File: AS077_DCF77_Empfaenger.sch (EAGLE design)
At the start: 82 parts, among them IC1 CA3130E, IC2 4093N, IC3 4538N, IC4 4093N, J1 Rückkopplung, J2 JUMPER_J5MM, J3 JUMPER_J5MM, Q1 34MM_PIEZO, T1 BC549C, T2 BF244A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

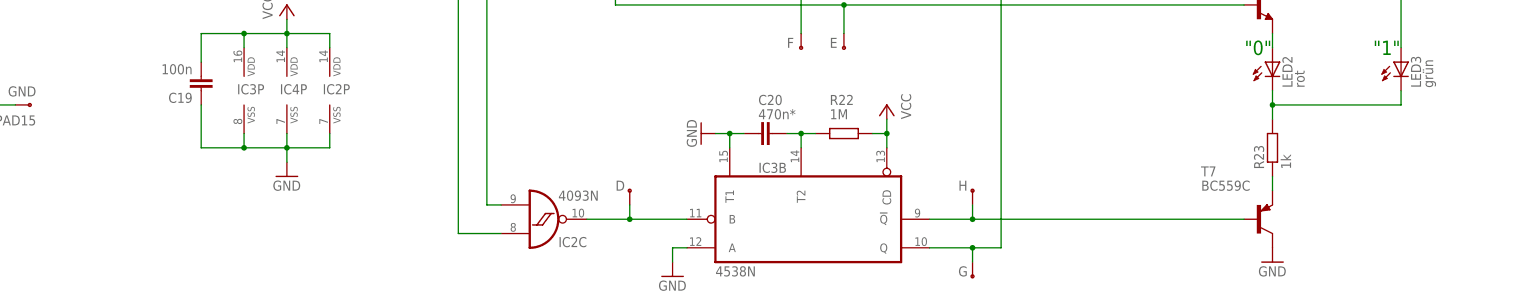
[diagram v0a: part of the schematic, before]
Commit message: * Renamed included library * Changed all references to new lib name
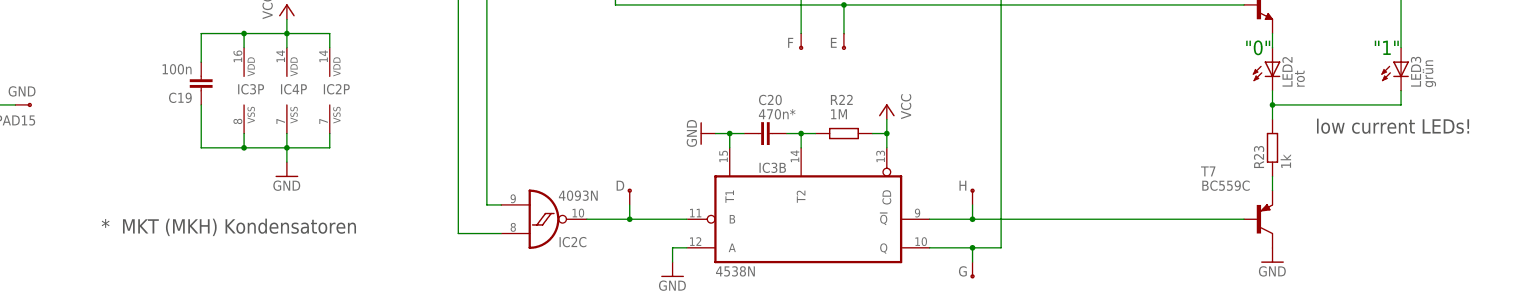
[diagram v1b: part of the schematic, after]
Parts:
- C1, C10, C16, C17, C19, C2, C4, C5, C6, C9: device 0027 DCF77-Empfänger:RCL_C-EU050-024X044 -> AS077_DCF77_Empfaenger:RCL_C-EU050-024X044
- C11, C13, C14, C15, C20, C7: device 0027 DCF77-Empfänger:RCL_C-EU075-032X103 -> AS077_DCF77_Empfaenger:RCL_C-EU075-032X103
- C12: device 0027 DCF77-Empfänger:RCL_CPOL-EUE5-6 -> AS077_DCF77_Empfaenger:RCL_CPOL-EUE5-6
- C18, C3: device 0027 DCF77-Empfänger:RCL_CPOL-EUE5-10.5 -> AS077_DCF77_Empfaenger:RCL_CPOL-EUE5-10.5
- C8: device 0027 DCF77-Empfänger:RCL_C-TRIMM808-7.5 -> AS077_DCF77_Empfaenger:RCL_C-TRIMM808-7.5
- D1, D2: device 0027 DCF77-Empfänger:DIODE_AA112 -> AS077_DCF77_Empfaenger:DIODE_AA112
- IC1: device 0027 DCF77-Empfänger:CA3130N -> AS077_DCF77_Empfaenger:CA3130N
- IC2, IC4: device 0027 DCF77-Empfänger:40XX_4093N -> AS077_DCF77_Empfaenger:40XX_4093N
- IC3: device 0027 DCF77-Empfänger:45XX_4538N -> AS077_DCF77_Empfaenger:45XX_4538N
- J1, J2, J3: device 0027 DCF77-Empfänger:JUMPER_J5MM -> AS077_DCF77_Empfaenger:JUMPER_J5MM
- LED1, LED2, LED3: device 0027 DCF77-Empfänger:LED_LED5MM -> AS077_DCF77_Empfaenger:LED_LED5MM
- PAD1, PAD10, PAD11, PAD12, PAD13, PAD14, PAD15, PAD16, PAD17, PAD18, PAD2, PAD3, PAD4, PAD5, PAD6, PAD7, PAD8, PAD9: device 0027 DCF77-Empfänger:WIREPAD_2.2/1.3 -> AS077_DCF77_Empfaenger:WIREPAD_2.2/1.3
- Q1: device 0027 DCF77-Empfänger:34MM_PIEZO -> AS077_DCF77_Empfaenger:34MM_PIEZO
- R1, R10, R11, R12, R13, R14, R15, R16, R19, R2, R20, R21, R4, R5, R6, R7, R8, R9: device 0027 DCF77-Empfänger:RCL_R-EU_0207/5V -> AS077_DCF77_Empfaenger:RCL_R-EU_0207/5V
- R17, R18, R22, R3: device 0027 DCF77-Empfänger:RCL_R-EU_0207/15 -> AS077_DCF77_Empfaenger:RCL_R-EU_0207/15
- R23: device 0027 DCF77-Empfänger:RCL_R-EU_0207/10 -> AS077_DCF77_Empfaenger:RCL_R-EU_0207/10
- T1, T3, T4: device 0027 DCF77-Empfänger:BC549C5.08 -> AS077_DCF77_Empfaenger:BC549C5.08
- T2: device 0027 DCF77-Empfänger:BF244A5.08 -> AS077_DCF77_Empfaenger:BF244A5.08
- T5, T6: device 0027 DCF77-Empfänger:BC549C2.54 -> AS077_DCF77_Empfaenger:BC549C2.54
- T7: device 0027 DCF77-Empfänger:BC559C5.08 -> AS077_DCF77_Empfaenger:BC559C5.08
- U$1: device 0027 DCF77-Empfänger:9V_SILKSCREEN -> AS077_DCF77_Empfaenger:9V_SILKSCREEN
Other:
- note added: "* MKT (MKH) Kondensatoren"
- note added: "low current LEDs!"

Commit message: * More schematic and layout cleanup
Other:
- note added: "22n unter der Platine"
- note added: "evtl. abgleichen"
- moved on the sheet: C18, IC4C, IC4D, PAD15, R20
